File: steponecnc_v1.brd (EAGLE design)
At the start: 101.6 x 83.8 mm, 35 parts

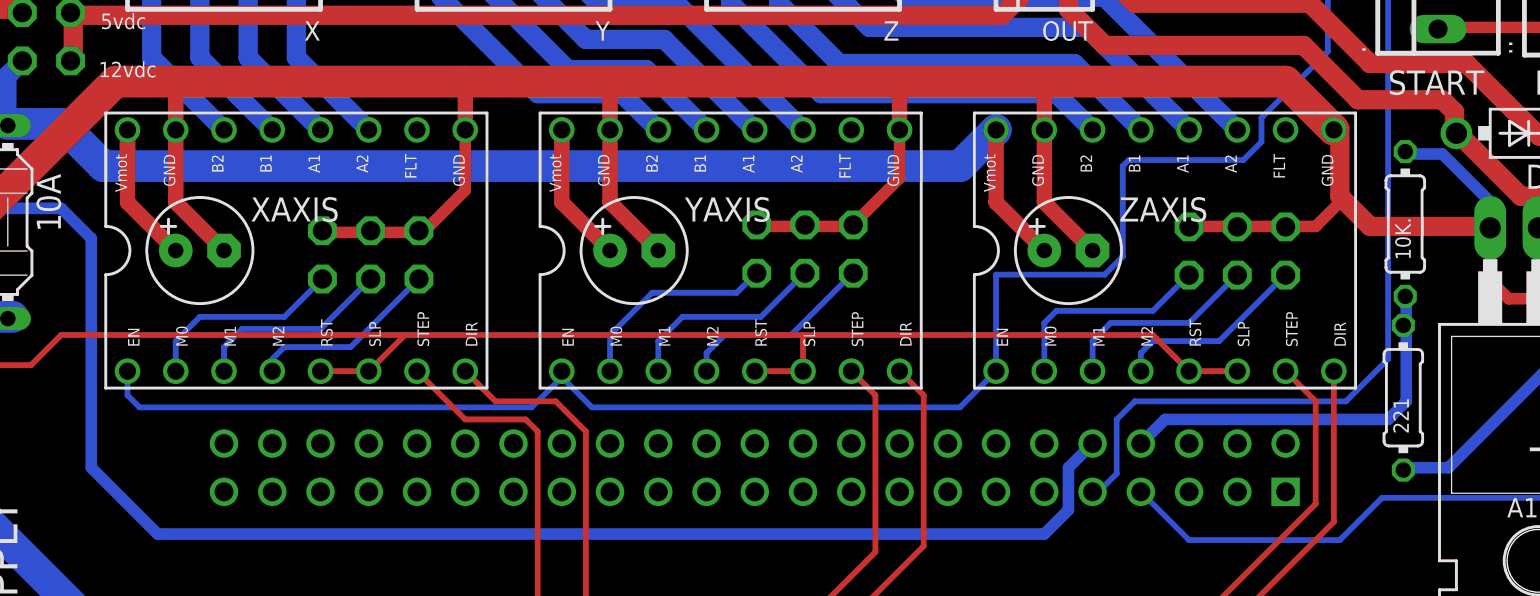
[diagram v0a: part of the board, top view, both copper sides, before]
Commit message: updated after initial build
still a work in progress but first version is built
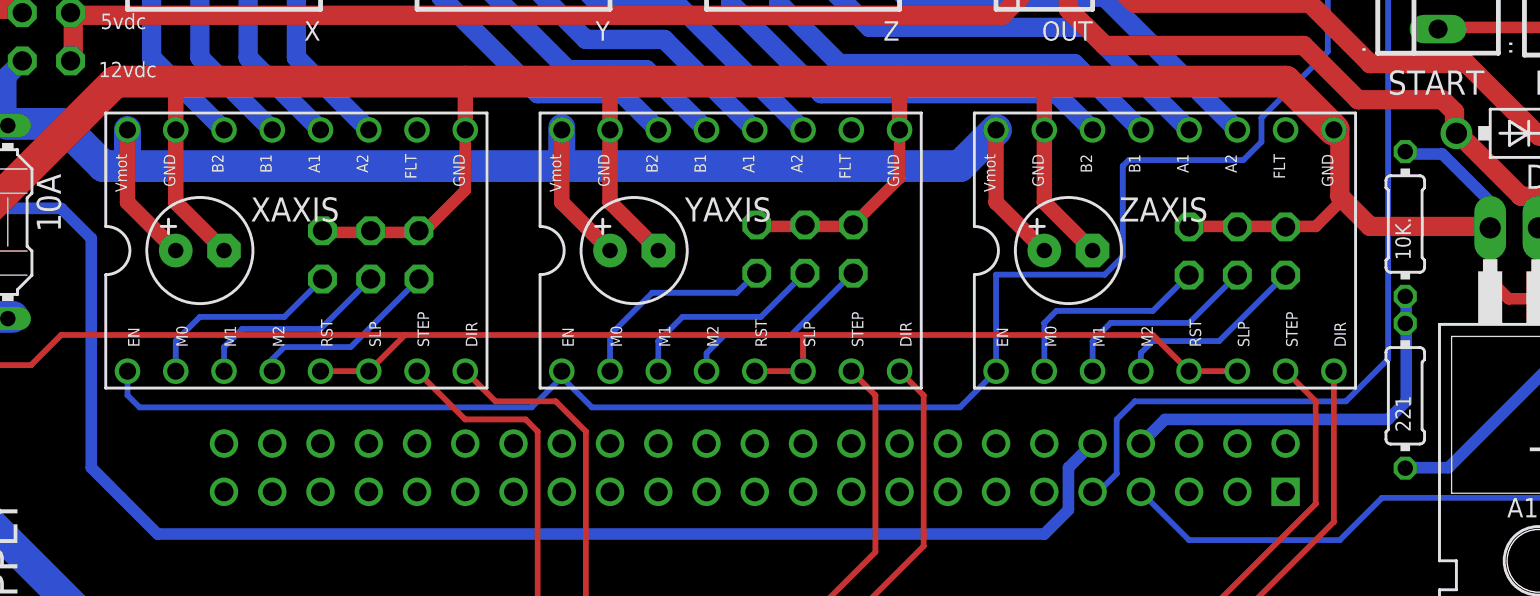
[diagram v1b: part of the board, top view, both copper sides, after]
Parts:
- moved 221 0.14 mm to (87.6, 56.5)
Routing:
- net S$18: track 83.5 -> 87.4 mm
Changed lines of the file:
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@@
 <element name="10K." library="resistor2" package="0204/7" value="" x="87.5792" y="65.532" rot="R90"/>
 <element name="D1" library="diode" package="DO41-7" value="" x="94.0816" y="70.3072" rot="R180"/>
-<element name="221" library="resistor2" package="0204/7" value="" x="87.4776" y="56.388" rot="R90"/>
+<element name="221" library="resistor2" package="0204/7" value="" x="87.5792" y="56.4896" rot="R90"/>
 </elements>
 <signals>
@@
 <wire x1="43.18" y1="70.485" x2="43.18" y2="66.675" width="0.8128" layer="1"/>
 <wire x1="43.18" y1="66.675" x2="45.72" y2="64.135" width="0.8128" layer="1"/>
-<wire x1="43.18" y1="68.58" x2="43.18" y2="70.485" width="0.8128" layer="16"/>
+<wire x1="43.18" y1="68.58" x2="43.18" y2="68.6816" width="0.8128" layer="16"/>
+<wire x1="43.18" y1="68.6816" x2="43.18" y2="70.485" width="0.8128" layer="16"/>
 <wire x1="13.97" y1="70.8025" x2="13.97" y2="73.3044" width="1.016" layer="16"/>
 <wire x1="13.97" y1="73.3044" x2="14.8336" y2="74.168" width="1.016" layer="16"/>
 <wire x1="13.97" y1="70.8025" x2="16.8275" y2="70.8025" width="1.6764" layer="16"/>
 <wire x1="16.8275" y1="70.8025" x2="19.05" y2="68.58" width="1.6764" layer="16"/>
+<wire x1="20.32" y1="70.5104" x2="20.32" y2="68.58" width="1.4224" layer="16"/>
+<wire x1="43.18" y1="70.612" x2="43.18" y2="68.6816" width="1.4224" layer="16"/>
 </signal>
 <signal name="S$51">

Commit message: Added Linuxcnc config
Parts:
- moved 221 0.14 mm to (87.5, 56.4)
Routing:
- net S$21: track 81.0 -> 54.3 mm
- net S$65: track 0.00 -> 6.15 mm
- net S$18: track 87.4 -> 83.5 mm
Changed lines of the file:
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@@
 <element name="10K." library="resistor2" package="0204/7" value="" x="87.5792" y="65.532" rot="R90"/>
 <element name="D1" library="diode" package="DO41-7" value="" x="94.0816" y="70.3072" rot="R180"/>
-<element name="221" library="resistor2" package="0204/7" value="" x="87.5792" y="56.4896" rot="R90"/>
+<element name="221" library="resistor2" package="0204/7" value="" x="87.4776" y="56.388" rot="R90"/>
 </elements>
 <signals>
@@
 <wire x1="43.18" y1="70.485" x2="43.18" y2="66.675" width="0.8128" layer="1"/>
 <wire x1="43.18" y1="66.675" x2="45.72" y2="64.135" width="0.8128" layer="1"/>
-<wire x1="43.18" y1="68.58" x2="43.18" y2="68.6816" width="0.8128" layer="16"/>
-<wire x1="43.18" y1="68.6816" x2="43.18" y2="70.485" width="0.8128" layer="16"/>
+<wire x1="43.18" y1="68.58" x2="43.18" y2="70.485" width="0.8128" layer="16"/>
 <wire x1="13.97" y1="70.8025" x2="13.97" y2="73.3044" width="1.016" layer="16"/>
 <wire x1="13.97" y1="73.3044" x2="14.8336" y2="74.168" width="1.016" layer="16"/>
 <wire x1="13.97" y1="70.8025" x2="16.8275" y2="70.8025" width="1.6764" layer="16"/>
 <wire x1="16.8275" y1="70.8025" x2="19.05" y2="68.58" width="1.6764" layer="16"/>
-<wire x1="20.32" y1="70.5104" x2="20.32" y2="68.58" width="1.4224" layer="16"/>
-<wire x1="43.18" y1="70.612" x2="43.18" y2="68.6816" width="1.4224" layer="16"/>
 </signal>
 <signal name="S$51">
@@
 <contactref element="DRVY" pad="SLP"/>
 <wire x1="55.88" y1="57.785" x2="55.88" y2="59.69" width="0.3048" layer="1"/>
-<wire x1="34.925" y1="59.69" x2="16.8275" y2="59.69" width="0.3048" layer="1"/>
-<wire x1="16.8275" y1="59.69" x2="15.24" y2="58.1025" width="0.3048" layer="1"/>
-<wire x1="15.24" y1="58.1025" x2="8.89" y2="58.1025" width="0.3048" layer="1"/>
 </signal>
 <signal name="S$22">
@@
 <wire x1="14.605" y1="76.835" x2="14.9225" y2="76.5175" width="1.016" layer="1"/>
 </signal>
+<signal name="S$65">
+<wire x1="68.58" y1="53.9496" x2="68.58" y2="55.88" width="0.4064" layer="1"/>
+<wire x1="68.58" y1="55.88" x2="67.8688" y2="56.5912" width="0.4064" layer="1"/>
+<wire x1="67.8688" y1="56.5912" x2="67.6656" y2="56.7944" width="0.4064" layer="1"/>
+<wire x1="67.4624" y1="59.6392" x2="67.4624" y2="56.9976" width="0.4064" layer="1"/>
+<wire x1="67.4624" y1="56.9976" x2="67.6656" y2="56.7944" width="0.4064" layer="1"/>
+</signal>
 </signals>

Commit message: changed how microstep jumpers are connected
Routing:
- net S$17: track 138.7 -> 115.7 mm
- net S$75: track 0.00 -> 8.93 mm
- net S$12: track 20.6 -> 12.1 mm
- net S$74: track 0.00 -> 6.65 mm
- net S$72: track 0.00 -> 6.25 mm
- net S$68: track 0.00 -> 5.08 mm
- net S$73: track 0.00 -> 4.98 mm
- net S$67: track 0.00 -> 4.98 mm
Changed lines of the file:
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@@
 <wire x1="68.58" y1="73.025" x2="81.28" y2="73.025" width="1.6764" layer="1"/>
 <wire x1="81.28" y1="73.025" x2="83.82" y2="70.485" width="1.6764" layer="1"/>
-<wire x1="38.1" y1="70.485" x2="38.1" y2="67.31" width="0.6096" layer="1"/>
-<wire x1="38.1" y1="67.31" x2="35.8775" y2="65.0875" width="0.6096" layer="1"/>
-<wire x1="35.8775" y1="65.0875" x2="30.48" y2="65.0875" width="0.6096" layer="1"/>
-<wire x1="60.96" y1="70.485" x2="60.96" y2="67.945" width="0.6096" layer="1"/>
-<wire x1="60.96" y1="67.945" x2="58.42" y2="65.405" width="0.6096" layer="1"/>
-<wire x1="58.42" y1="65.405" x2="53.6575" y2="65.405" width="0.6096" layer="1"/>
-<wire x1="53.6575" y1="65.405" x2="53.34" y2="65.7225" width="0.6096" layer="1"/>
-<wire x1="10.795" y1="64.135" x2="11.1125" y2="64.4525" width="1.6764" layer="1"/>
-<wire x1="11.1125" y1="64.4525" x2="19.685" y2="73.025" width="1.6764" layer="1"/>
-<wire x1="8.89" y1="62.23" x2="10.795" y2="64.135" width="1.6764" layer="1"/>
+<wire x1="8.89" y1="62.23" x2="19.685" y2="73.025" width="1.6764" layer="1"/>
 </signal>
 <signal name="S$18">
@@
 <wire x1="94.9325" y1="82.8675" x2="95.25" y2="82.55" width="0.3048" layer="16"/>
 </signal>
+<signal name="S$67">
+<wire x1="30.6832" y1="65.1256" x2="35.6616" y2="65.1256" width="0.4064" layer="16"/>
+</signal>
 <signal name="S$27">
 <wire x1="80.01" y1="69.85" x2="79.0575" y2="68.8975" width="0.3048" layer="16"/>
@@
 <wire x1="84.1375" y1="70.1675" x2="84.1375" y2="66.9925" width="1.016" layer="1"/>
 <wire x1="84.1375" y1="66.9925" x2="84.1375" y2="66.675" width="0.6096" layer="1"/>
-<wire x1="84.1375" y1="66.675" x2="82.8675" y2="65.405" width="0.6096" layer="1"/>
-<wire x1="82.8675" y1="65.405" x2="76.2" y2="65.405" width="0.6096" layer="1"/>
 <wire x1="92.075" y1="65.405" x2="85.725" y2="65.405" width="1.016" layer="1"/>
 <wire x1="85.725" y1="65.405" x2="84.1375" y2="66.9925" width="1.016" layer="1"/>
@@
 <wire x1="67.4624" y1="56.9976" x2="67.6656" y2="56.7944" width="0.4064" layer="1"/>
 </signal>
+<signal name="S$68">
+<wire x1="76.2" y1="65.4304" x2="81.28" y2="65.4304" width="0.4064" layer="16"/>
+</signal>
+<signal name="S$73">
+<wire x1="53.5432" y1="65.532" x2="58.5216" y2="65.532" width="0.4064" layer="16"/>
+</signal>
+<signal name="S$72">
+<wire x1="35.6616" y1="65.1256" x2="36.2712" y2="65.1256" width="0.4064" layer="1"/>
+<wire x1="36.2712" y1="65.1256" x2="36.8808" y2="64.516" width="0.4064" layer="1"/>
+<wire x1="36.8808" y1="64.516" x2="36.8808" y2="59.7408" width="0.4064" layer="1"/>
+</signal>
+<signal name="S$74">
+<wire x1="58.6232" y1="65.6336" x2="59.1312" y2="65.6336" width="0.4064" layer="1"/>
+<wire x1="59.1312" y1="65.6336" x2="59.7408" y2="65.024" width="0.4064" layer="1"/>
+<wire x1="59.7408" y1="65.024" x2="59.7408" y2="59.7408" width="0.4064" layer="1"/>
+</signal>
+<signal name="S$75">
+<wire x1="76.0984" y1="65.532" x2="75.692" y2="65.532" width="0.4064" layer="1"/>
+<wire x1="75.692" y1="65.532" x2="74.9808" y2="64.8208" width="0.4064" layer="1"/>
+<wire x1="74.9808" y1="64.8208" x2="74.9808" y2="59.0296" width="0.4064" layer="1"/>
+<wire x1="74.9808" y1="59.0296" x2="75.184" y2="58.8264" width="0.4064" layer="1"/>
+<wire x1="75.184" y1="58.8264" x2="75.2856" y2="58.7248" width="0.4064" layer="1"/>
+<wire x1="76.2" y1="57.8104" x2="75.2856" y2="58.7248" width="0.4064" layer="1"/>
+</signal>
 </signals>
